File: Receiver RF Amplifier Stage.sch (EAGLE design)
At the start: 16 parts, among them T1 2N2222

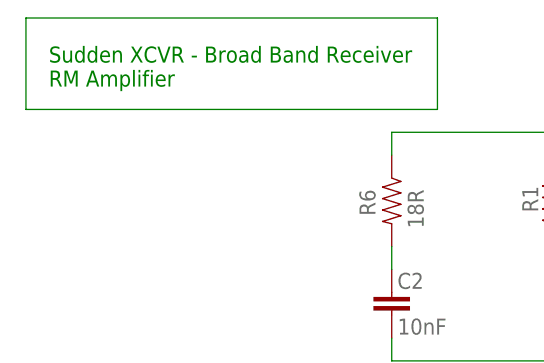
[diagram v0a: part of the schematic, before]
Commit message: Adding some images as well as updates
Adding some images as well as updates to the Receiver RF Amplifier Stage
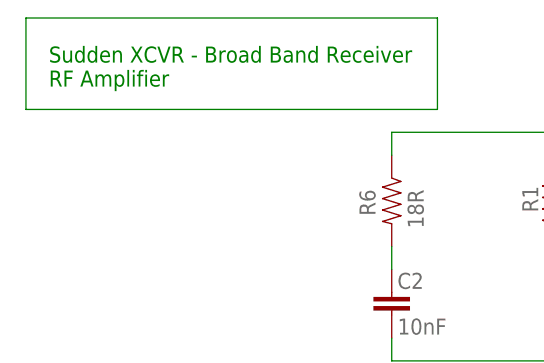
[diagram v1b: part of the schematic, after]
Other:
- note added: "Sudden XCVR - Broad Band Receiver RF Amplifier"
- note removed: "Sudden XCVR - Broad Band Receiver RM Amplifier"
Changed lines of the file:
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@@
 <plain>
 <text x="22.86" y="81.28" size="1.778" layer="91">Sudden XCVR - Broad Band Receiver
-RM Amplifier</text>
+RF Amplifier</text>
 <text x="38.1" y="10.16" size="1.778" layer="91">2 Bifilar Turns on FT-37-43 core
 #26 Wire</text>

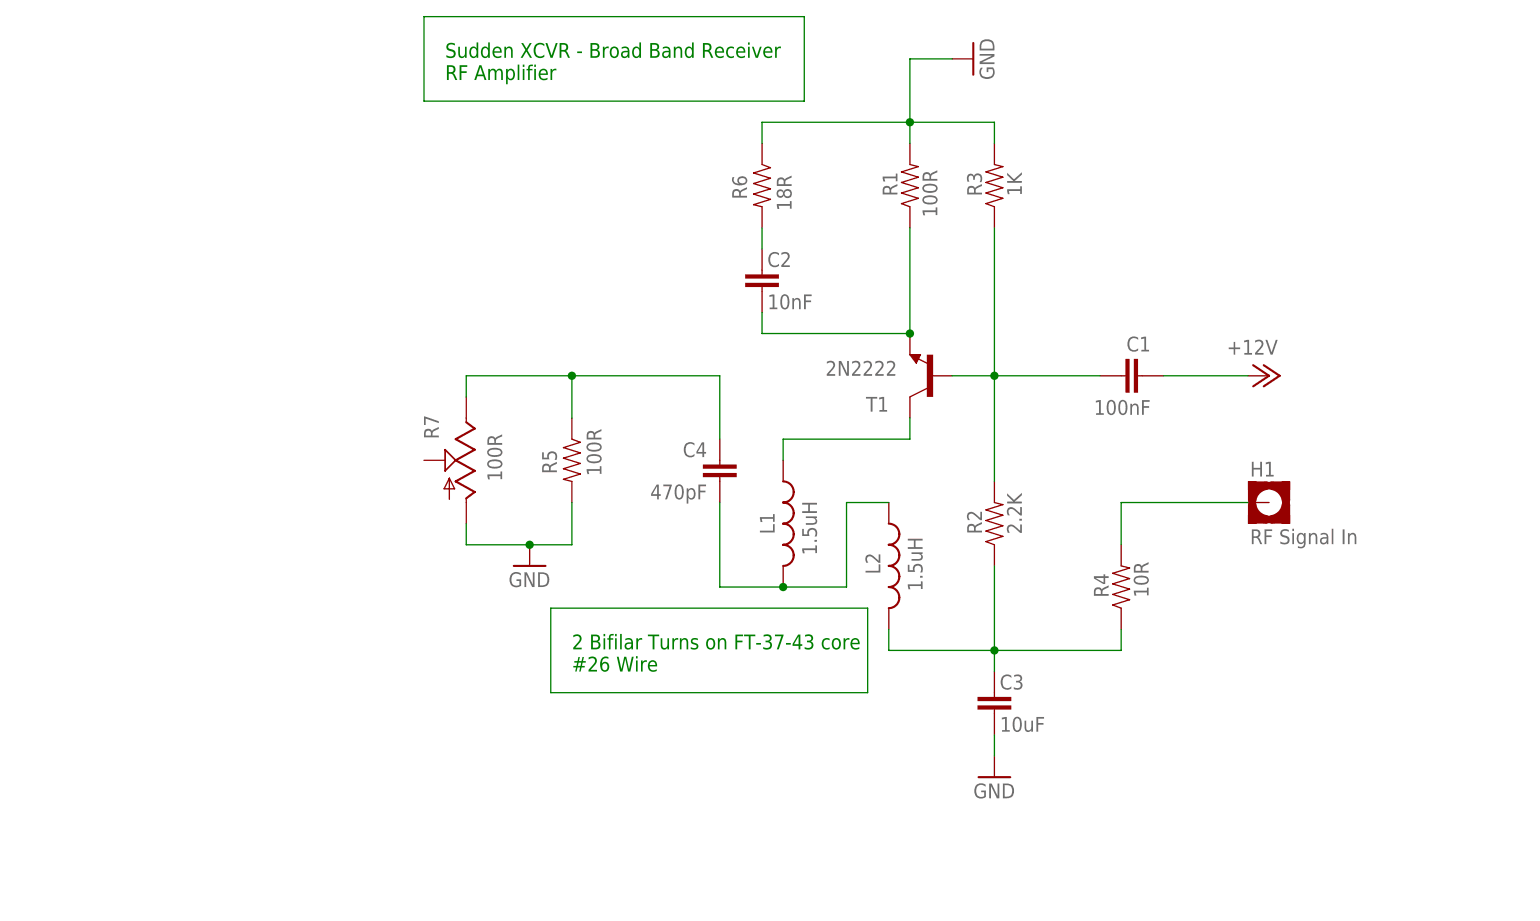
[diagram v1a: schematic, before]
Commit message: Updated schematic to have a bifilar winding
Updated schematic to have a bifilar winding or center tapped
transformer.

Also starting to work on the board.

On branch master
Your branch is up-to-date with 'origin/master'.

Changes to be committed:
       modified:   Receiver RF Amplifier Stage.b#1
       modified:   Receiver RF Amplifier Stage.b#2
       modified:   Receiver RF Amplifier Stage.b#3
       modified:   Receiver RF Amplifier Stage.b#4
       modified:   Receiver RF Amplifier Stage.b#5
       new file:   Receiver RF Amplifier Stage.b#6
       new file:   Receiver RF Amplifier Stage.b#7
       new file:   Receiver RF Amplifier Stage.b#8
       new file:   Receiver RF Amplifier Stage.b#9
       modified:   Receiver RF Amplifier Stage.brd
       modified:   Receiver RF Amplifier Stage.s#1
       modified:   Receiver RF Amplifier Stage.s#2
       modified:   Receiver RF Amplifier Stage.s#3
       modified:   Receiver RF Amplifier Stage.s#4
       modified:   Receiver RF Amplifier Stage.s#5
       modified:   Receiver RF Amplifier Stage.s#6
       modified:   Receiver RF Amplifier Stage.s#7
       modified:   Receiver RF Amplifier Stage.s#8
       new file:   Receiver RF Amplifier Stage.s#9
       modified:   Receiver RF Amplifier Stage.sch
       modified:   broadband_receiver_rf_amp.png
       modified:   eagle.epf
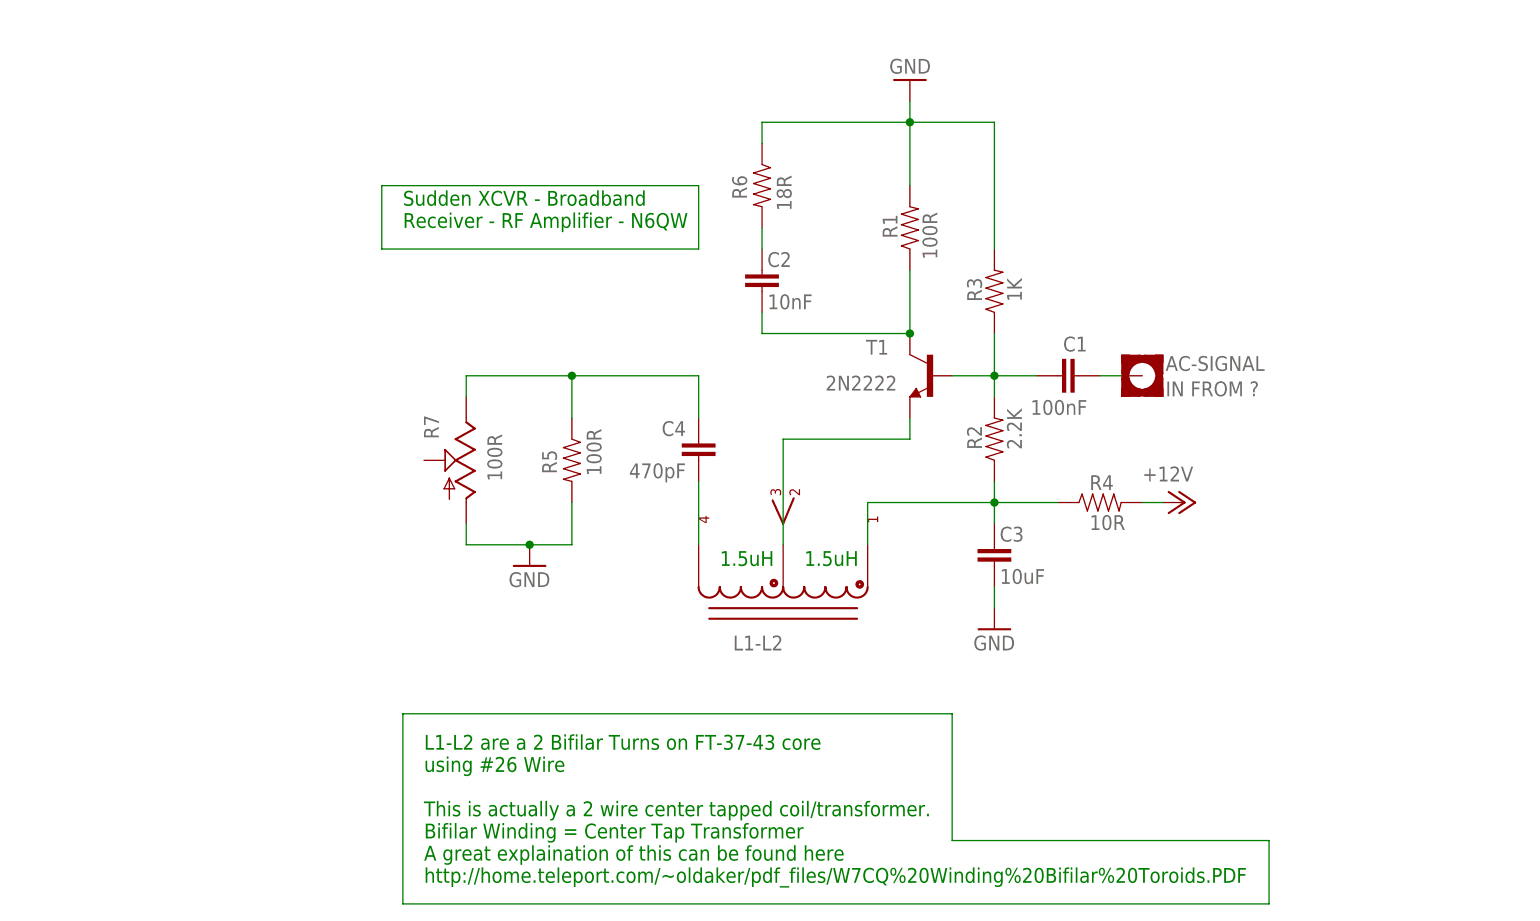
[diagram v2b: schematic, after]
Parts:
- removed H1: RF Signal In, jim_muppet_parts:MOUNT-PAD-SQUARE4.5
- removed L1, L2: 1.5uH, SparkFun-Passives:INDUCTOR
- added AC-SIGNAL: IN FROM ?, jim_muppet_parts:MOUNT-PAD-SQUARE4.5
- added L1-L2: T37-43_BIFILAR_TORIODBIFILAR-COIL/TRANSFORMER, jim_muppet_parts:T37-43_BIFILAR_TORIODBIFILAR-COIL/TRANSFORMER
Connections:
- net +12V: now also R4.2; no longer C1.2
- net N$3: now also T1.C; no longer T1.E
- net N$5: now also L1-L2.C2A, T1.E; no longer L1.1, T1.C
- net N$6: now also L1-L2.C3A; no longer L1.2, L2.1
- net N$7: now also L1-L2.C1A; no longer L2.2
- net N$9: now also AC-SIGNAL.MOUNT, C1.2; no longer H1.MOUNT, R4.2
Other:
- note added: "1.5uH"
- note added: "L1-L2 are a 2 Bifilar Turns on FT-37-43 core using #26 Wire This is actually a 2 wire center tapped coil/transformer. Bifilar Winding = Center Tap Transformer A great explaination of this can be found here http://home.teleport.com/~oldaker/pdf_files/W7CQ%20Winding%20Bifilar%20Toroids.PDF"
- note added: "Sudden XCVR - Broadband Receiver - RF Amplifier - N6QW"
- note removed: "2 Bifilar Turns on FT-37-43 core #26 Wire"
- note removed: "Sudden XCVR - Broad Band Receiver RF Amplifier"
- moved on the sheet: C1, C3, C4, R1, R2, R3, R4, T1

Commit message: Lots of changes.
Recreated the IF Schema and a new board to look like the photo

On branch master
Changes to be committed:
       modified:   Receiver RF Amplifier Stage.b#1
       modified:   Receiver RF Amplifier Stage.b#2
       modified:   Receiver RF Amplifier Stage.b#3
       modified:   Receiver RF Amplifier Stage.b#4
       modified:   Receiver RF Amplifier Stage.b#5
       modified:   Receiver RF Amplifier Stage.b#6
       modified:   Receiver RF Amplifier Stage.b#7
       modified:   Receiver RF Amplifier Stage.b#8
       modified:   Receiver RF Amplifier Stage.b#9
       modified:   Receiver RF Amplifier Stage.brd
       modified:   Receiver RF Amplifier Stage.s#1
       modified:   Receiver RF Amplifier Stage.s#2
       modified:   Receiver RF Amplifier Stage.s#3
       modified:   Receiver RF Amplifier Stage.s#4
       modified:   Receiver RF Amplifier Stage.s#5
       modified:   Receiver RF Amplifier Stage.s#6
       modified:   Receiver RF Amplifier Stage.s#7
       modified:   Receiver RF Amplifier Stage.s#8
       modified:   Receiver RF Amplifier Stage.s#9
       modified:   Receiver RF Amplifier Stage.sch
       modified:   Sudden_XCVR_IF_Module.b#1
       modified:   Sudden_XCVR_IF_Module.b#2
       modified:   Sudden_XCVR_IF_Module.b#3
       modified:   Sudden_XCVR_IF_Module.b#4
       modified:   Sudden_XCVR_IF_Module.b#5
       modified:   Sudden_XCVR_IF_Module.b#6
       modified:   Sudden_XCVR_IF_Module.b#7
       modified:   Sudden_XCVR_IF_Module.brd
       new file:   Sudden_XCVR_IF_Module_Schematic_like_board_layout.b#1
       new file:   Sudden_XCVR_IF_Module_Schematic_like_board_layout.b#2
       new file:   Sudden_XCVR_IF_Module_Schematic_like_board_layout.b#3
       new file:   Sudden_XCVR_IF_Module_Schematic_like_board_layout.brd
       new file:   Sudden_XCVR_IF_Module_Schematic_like_board_layout.s#1
       new file:   Sudden_XCVR_IF_Module_Schematic_like_board_layout.s#2
       new file:   Sudden_XCVR_IF_Module_Schematic_like_boa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
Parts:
- removed R7: 100R, jim_muppet_parts:POTENTIOMETER-TRIMCA14V
- added AC-SIGNAL-OUT: Output from Center Wiper, jim_muppet_parts:MOUNT-PAD-SQUARE4.5
- added R11: (no value), jim_muppet_parts:POTENTIOMETER-TRIMCT6
- T1: device jim_muppet_parts:2N3904 -> jim_muppet_parts:2N2222
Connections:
- new net N$12: C2.1, R1.1, T1.E
- net GND: now also R11.E; no longer R7.A
- net N$3: now also AC-SIGNAL-OUT.MOUNT, R11.S; no longer C2.1, R1.1, T1.C
- net N$5: now also T1.C; no longer T1.E
- net N$8: now also R11.A; no longer R7.E
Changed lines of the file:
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@@
 </variantdefs>
 <classes>
-<class number="0" name="default" width="0" drill="0">
+<class number="0" name="default" width="0.9398" drill="0">
+<clearance class="0" value="0.889"/>
 </class>
 </classes>
 <parts>
-<part name="T1" library="jim_muppet_parts" deviceset="2N3904" device="" package3d_urn="urn:adsk.eagle:package:29893/2" value="2N2222"/>
 <part name="R1" library="jim_muppet_parts" deviceset="RESISTOR-MUPPET" device="MEDIUM-RESISTOR-PADS" value="100R"/>
 <part name="R2" library="jim_muppet_parts" deviceset="RESISTOR-MUPPET" device="MEDIUM-RESISTOR-PADS" value="2.2K"/>
@@
 <part name="C3" library="jim_muppet_parts" deviceset="CAP-MEDIUM-MUPPET" device="" value="10uF"/>
 <part name="C4" library="jim_muppet_parts" deviceset="CAP-MEDIUM-MUPPET" device="" value="470pF"/>
-<part name="R7" library="jim_muppet_parts" deviceset="POTENTIOMETER-TRIM" device="CA14V" package3d_urn="urn:adsk.eagle:package:22695/1" value="100R"/>
 <part name="GND1" library="supply1" library_urn="urn:adsk.eagle:library:371" deviceset="GND" device=""/>
 <part name="GND4" library="supply1" library_urn="urn:adsk.eagle:library:371" deviceset="GND" device=""/>
@@
 <attribute name="SPICEPREFIX" value="A"/>
 </part>
+<part name="AC-SIGNAL-OUT" library="jim_muppet_parts" deviceset="MOUNT-PAD-SQUARE" device="4.5" package3d_urn="urn:adsk.eagle:package:14295/1" value="Output from Center Wiper"/>
+<part name="R11" library="jim_muppet_parts" deviceset="POTENTIOMETER-TRIM" device="CT6" package3d_urn="urn:adsk.eagle:package:22692/1"/>
+<part name="T1" library="jim_muppet_parts" deviceset="2N2222" device="" package3d_urn="urn:adsk.eagle:package:28728/1"/>
 </parts>
 <sheets>
@@
 </plain>
 <instances>
-<instance part="T1" gate="G1" x="81.28" y="45.72" smashed="yes" rot="MR0">
-<attribute name="NAME" x="76.2" y="48.26" size="1.778" layer="95" rot="MR0"/>
-<attribute name="VALUE" x="68.58" y="45.72" size="1.778" layer="96" rot="MR180"/>
-</instance>
 <instance part="R1" gate="G$1" x="78.74" y="63.5" smashed="yes" rot="R90">
 <attribute name="NAME" x="77.2414" y="62.23" size="1.778" layer="95" rot="R90"/>
@@
 <instance part="R2" gate="G$1" x="88.9" y="38.1" smashed="yes" rot="R90">
 <attribute name="NAME" x="87.4014" y="36.83" size="1.778" layer="95" rot="R90"/>
-<attribute name="VALUE" x="92.202" y="36.83" size="1.778" layer="96" rot="R90"/>
+<attribute name="VALUE" x="92.202" y="34.29" size="1.778" layer="96" rot="R90"/>
 </instance>
 <instance part="R3" gate="G$1" x="88.9" y="55.88" smashed="yes" rot="R90">
@@
 <attribute name="VALUE" x="51.816" y="35.179" size="1.778" layer="96" rot="R180"/>
 </instance>
-<instance part="R7" gate="G$1" x="25.4" y="35.56" smashed="yes" rot="MR0">
-<attribute name="NAME" x="20.32" y="38.1" size="1.778" layer="95" rot="MR90"/>
-<attribute name="VALUE" x="27.94" y="33.02" size="1.778" layer="96" rot="MR90"/>
-</instance>
 <instance part="GND1" gate="1" x="88.9" y="15.24" smashed="yes">
 <attribute name="VALUE" x="86.36" y="12.7" size="1.778" layer="96"/>
@@
 <attribute name="NAME" x="109.474" y="46.3042" size="1.778" layer="95"/>
 <attribute name="VALUE" x="109.474" y="43.2562" size="1.778" layer="96"/>
+</instance>
+<instance part="AC-SIGNAL-OUT" gate="G$1" x="12.7" y="35.56" smashed="yes" rot="R180">
+<attribute name="NAME" x="9.906" y="34.9758" size="1.778" layer="95" rot="R180"/>
+<attribute name="VALUE" x="9.906" y="38.0238" size="1.778" layer="96" rot="R180"/>
+</instance>
+<instance part="R11" gate="G$1" x="25.4" y="35.56" smashed="yes" rot="R180">
+<attribute name="NAME" x="30.48" y="38.1" size="1.778" layer="95" rot="R270"/>
+<attribute name="VALUE" x="27.94" y="38.1" size="1.778" layer="96" rot="R270"/>
+</instance>
+<instance part="T1" gate="G$1" x="81.28" y="45.72" smashed="yes" rot="R180">
+<attribute name="NAME" x="76.2" y="45.72" size="1.778" layer="95" rot="R180"/>
+<attribute name="VALUE" x="76.2" y="48.26" size="1.778" layer="96" rot="R180"/>
 </instance>
 </instances>
@@
 <junction x="88.9" y="45.72"/>
 <wire x1="88.9" y1="45.72" x2="88.9" y2="50.8" width="0.1524" layer="91"/>
-<pinref part="T1" gate="G1" pin="B"/>
 <wire x1="83.82" y1="45.72" x2="88.9" y2="45.72" width="0.1524" layer="91"/>
+<pinref part="T1" gate="G$1" pin="B"/>
 </segment>
 </net>
 <net name="GND" class="0">
 <segment>
-<pinref part="R7" gate="G$1" pin="A"/>
-<wire x1="25.4" y1="27.94" x2="25.4" y2="25.4" width="0.1524" layer="91"/>
 <pinref part="GND4" gate="1" pin="GND"/>
-<wire x1="25.4" y1="25.4" x2="33.02" y2="25.4" width="0.1524" layer="91"/>
 <pinref part="R5" gate="G$1" pin="2"/>
 <wire x1="33.02" y1="25.4" x2="38.1" y2="25.4" width="0.1524" layer="91"/>
 <wire x1="38.1" y1="25.4" x2="38.1" y2="30.48" width="0.1524" layer="91"/>
+<pinref part="R11" gate="G$1" pin="E"/>
+<wire x1="33.02" y1="25.4" x2="25.4" y2="25.4" width="0.1524" layer="91"/>
+<wire x1="25.4" y1="25.4" x2="25.4" y2="27.94" width="0.1524" layer="91"/>
 <junction x="33.02" y="25.4"/>
 </segment>
@@
 </segment>
 </net>
-<net name="N$3" class="0">
-<segment>
-<pinref part="C2" gate="G$1" pin="1"/>
-<wire x1="60.96" y1="50.8" x2="60.96" y2="53.34" width="0.1524" layer="91"/>
-<pinref part="T1" gate="G1" pin="C"/>
-<wire x1="78.74" y1="50.8" x2="60.96" y2="50.8" width="0.1524" layer="91"/>
-<pinref part="R1" gate="G$1" pin="1"/>
-<wire x1="78.74" y1="50.8" x2="78.74" y2="58.42" width="0.1524" layer="91"/>
-<junction x="78.74" y="50.8"/>
-</segment>
-</net>
 <net name="N$4" class="0">
 <segment>
@@
 <net name="N$5" class="0">
 <segment>
-<pinref part="T1" gate="G1" pin="E"/>
-<wire x1="78.74" y1="40.64" x2="78.74" y2="38.1" width="0.1524" layer="91"/>
 <pinref part="L1-L2" gate="G$1" pin="C2A"/>
 <wire x1="63.5" y1="25.4" x2="63.5" y2="38.1" width="0.1524" layer="91"/>
 <wire x1="63.5" y1="38.1" x2="78.74" y2="38.1" width="0.1524" layer="91"/>
+<wire x1="78.74" y1="40.64" x2="78.74" y2="38.1" width="0.1524" layer="91"/>
+<pinref part="T1" gate="G$1" pin="C"/>
 </segment>
 </net>
@@
 <wire x1="53.34" y1="40.64" x2="53.34" y2="45.72" width="0.1524" layer="91"/>
 <wire x1="53.34" y1="45.72" x2="38.1" y2="45.72" width="0.1524" layer="91"/>
-<pinref part="R7" gate="G$1" pin="E"/>
-<wire x1="38.1" y1="45.72" x2="25.4" y2="45.72" width="0.1524" layer="91"/>
-<wire x1="25.4" y1="45.72" x2="25.4" y2="43.18" width="0.1524" layer="91"/>
 <pinref part="R5" gate="G$1" pin="1"/>
 <wire x1="38.1" y1="40.64" x2="38.1" y2="45.72" width="0.1524" layer="91"/>
+<pinref part="R11" gate="G$1" pin="A"/>
+<wire x1="25.4" y1="43.18" x2="25.4" y2="45.72" width="0.1524" layer="91"/>
+<wire x1="25.4" y1="45.72" x2="38.1" y2="45.72" width="0.1524" layer="91"/>
 <junction x="38.1" y="45.72"/>
 </segment>
@@
 </segment>
 </net>
+<net name="N$12" class="0">
+<segment>
+<pinref part="C2" gate="G$1" pin="1"/>
+<wire x1="60.96" y1="50.8" x2="60.96" y2="53.34" width="0.1524" layer="91"/>
+<wire x1="60.96" y1="50.8" x2="78.74" y2="50.8" width="0.1524" layer="91"/>
+<pinref part="R1" gate="G$1" pin="1"/>
+<wire x1="78.74" y1="58.42" x2="78.74" y2="50.8" width="0.1524" layer="91"/>
+<pinref part="T1" gate="G$1" pin="E"/>
+<junction x="78.74" y="50.8"/>
+</segment>
+</net>
+<net name="N$3" class="0">
+<segment>
+<pinref part="R11" gate="G$1" pin="S"/>
+<pinref part="AC-SIGNAL-OUT" gate="G$1" pin="MOUNT"/>
+<wire x1="20.32" y1="35.56" x2="15.24" y2="35.56" width="0.1524" layer="91"/>
+</segment>
+</net>
